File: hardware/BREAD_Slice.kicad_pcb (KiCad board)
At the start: 4 copper layers, 100 x 145 mm, 21 parts, among them J1 Conn_01x10_Socket, SW1 SW_DIP_x04, U1 AP63205

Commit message: did schematic
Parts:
- added J1: Screw_Terminal_01x02, TerminalBlock:TerminalBlock_MaiXu_MX126-5.0-02P_1x02_P5.00mm, F.Cu at (186.0, 121.2)
- added J3: PCIE-036-02-X-D-TH, KMLib_Connectors:SAMTEC_PCIE-036-02-X-D-TH, F.Cu at (144.0, 89.7)
- added J4: PCIE-036-02-X-D-TH, KMLib_Connectors:SAMTEC_PCIE-036-02-X-D-TH, F.Cu at (143.8, 67.7)
- added J5: PCIE-036-02-X-D-TH, KMLib_Connectors:SAMTEC_PCIE-036-02-X-D-TH, F.Cu at (143.8, 50.2)
- added J6: PCIE-036-02-X-D-TH, KMLib_Connectors:SAMTEC_PCIE-036-02-X-D-TH, F.Cu at (143.5, 33.2)
- added R1: 10k, Resistor_SMD:R_0603_1608Metric_Pad0.98x0.95mm_HandSolder, F.Cu at (145.8, 97.5)
- added R2: 10k, Resistor_SMD:R_0603_1608Metric_Pad0.98x0.95mm_HandSolder, F.Cu at (145.1, 75.2)
- added R3: 10k, Resistor_SMD:R_0603_1608Metric_Pad0.98x0.95mm_HandSolder, F.Cu at (144.8, 58.5)
- added R4: 10k, Resistor_SMD:R_0603_1608Metric_Pad0.98x0.95mm_HandSolder, F.Cu at (144.8, 40.5)
- added SW1: SW_SPDT, Button_Switch_THT:SW_Slide-03_Wuerth-WS-SLTV_10x2.5x6.4_P2.54mm, F.Cu at (177.2, 131.8)
- renumbered A2 to A1, J1 to J2, SW1 to SW2
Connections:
- net /slice_template/I2C0_CLK/GPIO21 renamed /DIR3
- net /slice_template/I2C0_SDA/GPIO20 renamed /STEP3
- A1 pad 10: /slice_template/GPIO7 -> /Stepper_card/SCL
- A1 pad 11: /slice_template/GPIO8 -> /STEP0
- A1 pad 12: /slice_template/GPIO9 -> /DIR0
- A1 pad 14: /slice_template/GPIO10 -> /CS0
- A1 pad 15: /slice_template/GPIO11 -> /STATUS0
- A1 pad 16: /slice_template/GPIO12 -> /STEP1
- A1 pad 17: /slice_template/GPIO13 -> /DIR1
- A1 pad 19: /slice_template/GPIO14 -> /CS1
- A1 pad 20: /slice_template/GPIO15 -> /STATUS1
- A1 pad 21: /slice_template/GPIO16 -> /STEP2
- A1 pad 22: /slice_template/GPIO17 -> /DIR2
- A1 pad 24: /slice_template/GPIO18 -> /CS2
- A1 pad 25: /slice_template/GPIO19 -> /STATUS2
- A1 pad 32: /slice_template/GPIO27_ADC1 -> /CS3
- A1 pad 34: /slice_template/GPIO28_ADC2 -> /STATUS3
- A1 pad 4: /slice_template/GPIO2 -> /SCLK
- A1 pad 5: /slice_template/GPIO3 -> /COPI
- A1 pad 6: /slice_template/GPIO4 -> /CIPO
- A1 pad 9: /slice_template/GPIO6 -> /Stepper_card/SDA

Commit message: more routing
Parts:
- removed SW1: SW_SPDT, Button_Switch_THT:SW_Slide-03_Wuerth-WS-SLTV_10x2.5x6.4_P2.54mm
- moved J4 10.3 mm to (151.0, 75.0)
- moved R2 9.68 mm to (151.5, 82.5), turned to -90 degrees
- moved J3 8.80 mm to (151.0, 95.0)
- moved J5 8.71 mm to (151.0, 55.0)
- moved R3 7.77 mm to (151.5, 62.5), turned to -90 degrees
- moved J6 7.72 mm to (151.0, 35.0)
- moved R1 7.62 mm to (151.5, 102.5), turned to -90 degrees
- moved R4 6.96 mm to (151.5, 42.5), turned to -90 degrees
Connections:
- J1 pad 1: Net-(J1-Pin_1) -> VM
- J3 pad A11: unconnected-(J3-PadA11) -> +3V3
- J3 pad A12: +3V3 -> VM
- J3 pad A3: /CIPO -> /SCLK
- J3 pad A5: /SCLK -> /CIPO
- J3 pad B11: unconnected-(J3-PadB11) -> +3V3
- J3 pad B12: +3V3 -> VM
- J3 pad B3: unconnected-(J3-PadB3) -> /SCLK
- J3 pad B4: unconnected-(J3-PadB4) -> /COPI
- J3 pad B5: unconnected-(J3-PadB5) -> /CIPO
- J3 pad B7: unconnected-(J3-PadB7) -> /Stepper_card/SDA
- J3 pad B8: unconnected-(J3-PadB8) -> /Stepper_card/SCL
- J4 pad A11: unconnected-(J4-PadA11) -> +3V3
- J4 pad A12: +3V3 -> VM
- J4 pad A3: /CIPO -> /SCLK
- J4 pad A5: /SCLK -> /CIPO
- J4 pad B11: unconnected-(J4-PadB11) -> +3V3
- J4 pad B12: +3V3 -> VM
- J4 pad B3: unconnected-(J4-PadB3) -> /SCLK
- J4 pad B4: unconnected-(J4-PadB4) -> /COPI
- J4 pad B5: unconnected-(J4-PadB5) -> /CIPO
- J4 pad B7: unconnected-(J4-PadB7) -> /Stepper_card/SDA
- J4 pad B8: unconnected-(J4-PadB8) -> /Stepper_card/SCL
- J5 pad A11: unconnected-(J5-PadA11) -> +3V3
- J5 pad A12: +3V3 -> VM
- J5 pad A3: /CIPO -> /SCLK
- J5 pad A5: /SCLK -> /CIPO
- J5 pad B11: unconnected-(J5-PadB11) -> +3V3
- J5 pad B12: +3V3 -> VM
- J5 pad B3: unconnected-(J5-PadB3) -> /SCLK
- J5 pad B4: unconnected-(J5-PadB4) -> /COPI
- J5 pad B5: unconnected-(J5-PadB5) -> /CIPO
- J5 pad B7: unconnected-(J5-PadB7) -> /Stepper_card/SDA
- J5 pad B8: unconnected-(J5-PadB8) -> /Stepper_card/SCL
- J6 pad A11: unconnected-(J6-PadA11) -> +3V3
- J6 pad A12: +3V3 -> VM
- J6 pad A3: /CIPO -> /SCLK
- J6 pad A5: /SCLK -> /CIPO
- J6 pad B11: unconnected-(J6-PadB11) -> +3V3
- J6 pad B12: +3V3 -> VM
- J6 pad B3: unconnected-(J6-PadB3) -> /SCLK
- J6 pad B4: unconnected-(J6-PadB4) -> /COPI
- J6 pad B5: unconnected-(J6-PadB5) -> /CIPO
- J6 pad B7: unconnected-(J6-PadB7) -> /Stepper_card/SDA
- J6 pad B8: unconnected-(J6-PadB8) -> /Stepper_card/SCL
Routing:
- net /SCLK: track 0.00 -> 126.7 mm
- net /COPI: track 0.00 -> 125.7 mm
- net VM: track 0.00 -> 121.4 mm
- net /CIPO: track 0.00 -> 120.8 mm
- net /Stepper_card/SDA: track 0.00 -> 112.3 mm
- net /Stepper_card/SCL: track 0.00 -> 111.4 mm
- net /STATUS2: track 0.00 -> 82.9 mm
- net /CS2: track 0.00 -> 82.5 mm
- net /DIR2: track 0.00 -> 79.1 mm
- net /STEP2: track 0.00 -> 77.6 mm
- net /STEP1: track 0.00 -> 63.3 mm
- net /DIR1: track 0.00 -> 58.6 mm
- net /CS1: track 0.00 -> 50.7 mm
- net /STEP0: track 0.00 -> 47.3 mm
- net /STATUS1: track 0.00 -> 46.4 mm
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
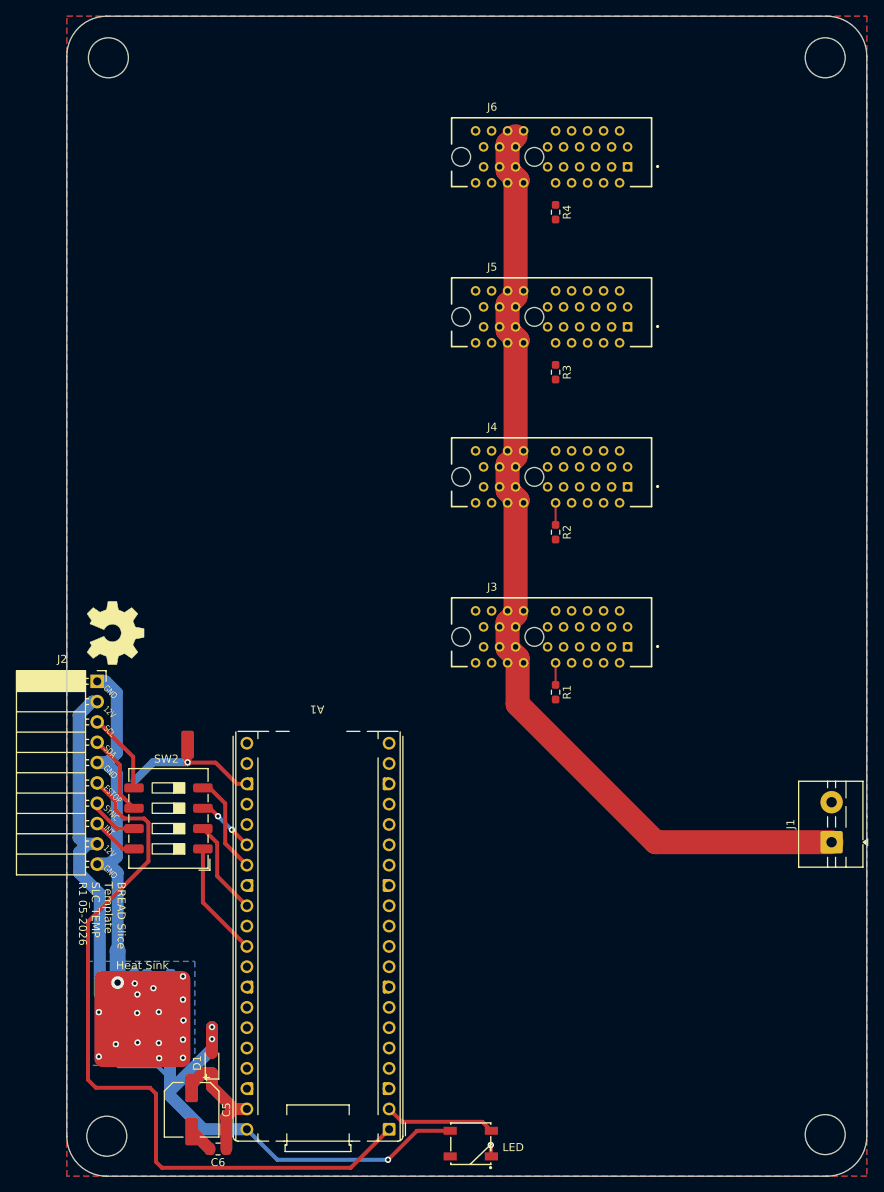
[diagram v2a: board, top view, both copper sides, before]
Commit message: finished initial routing
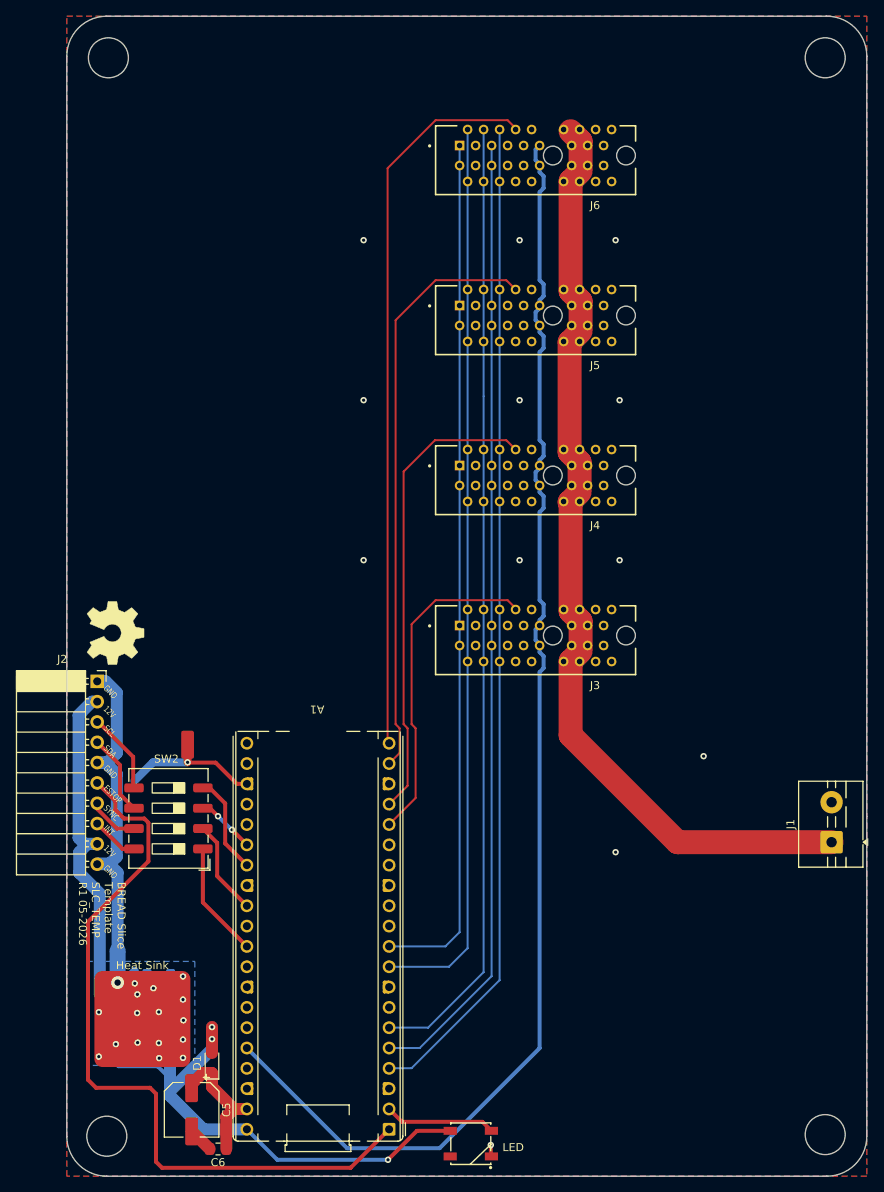
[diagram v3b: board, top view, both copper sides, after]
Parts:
- removed R1, R2, R3, R4: 10k, Resistor_SMD:R_0603_1608Metric_Pad0.98x0.95mm_HandSolder
- moved J3 2.24 mm to (149.0, 96.0), turned to 180 degrees
- moved J4 2.24 mm to (149.0, 76.0), turned to 180 degrees
- moved J5 2.24 mm to (149.0, 56.0), turned to 180 degrees
- moved J6 2.24 mm to (149.0, 36.0), turned to 180 degrees
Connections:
- A1 pad 11: /STEP0 -> /STEP3
- A1 pad 12: /DIR0 -> /STEP2
- A1 pad 14: /CS0 -> /STEP1
- A1 pad 15: /STATUS0 -> /STEP0
- A1 pad 16: /STEP1 -> /DIR0
- A1 pad 19: /CS1 -> /DIR2
- A1 pad 20: /STATUS1 -> /DIR3
- A1 pad 21: /STEP2 -> /CS3
- A1 pad 22: /DIR2 -> /CS2
- A1 pad 24: /CS2 -> /CS1
- A1 pad 25: /STATUS2 -> /CS0
- A1 pad 26: /STEP3 -> /slice_template/I2C0_SDA/GPIO20
- A1 pad 27: /DIR3 -> /slice_template/I2C0_CLK/GPIO21
- A1 pad 32: /CS3 -> /slice_template/GPIO27_ADC1
- A1 pad 34: /STATUS3 -> /slice_template/GPIO28_ADC2
- J3 pad A1: /STEP0 -> /Stepper_card/SCL
- J3 pad A10: /STATUS0 -> unconnected-(J3-PadA10)
- J3 pad A2: /DIR0 -> /Stepper_card/SDA
- J3 pad A3: /SCLK -> /CS0
- J3 pad A4: /COPI -> /CIPO
- J3 pad A5: /CIPO -> /COPI
- J3 pad A6: /CS0 -> /SCLK
- J3 pad A7: /Stepper_card/SDA -> /STEP0
- J3 pad A8: /Stepper_card/SCL -> /DIR0
- J3 pad A9: +3V3 -> unconnected-(J3-PadA9)
- J3 pad B1: /Stepper_card/nFAULT -> /Stepper_card/SCL
- J3 pad B2: unconnected-(J3-PadB2) -> /Stepper_card/SDA
- J3 pad B3: /SCLK -> unconnected-(J3-PadB3)
- J3 pad B4: /COPI -> /CIPO
- J3 pad B5: /CIPO -> /COPI
- J3 pad B6: unconnected-(J3-PadB6) -> /SCLK
- J3 pad B7: /Stepper_card/SDA -> unconnected-(J3-PadB7)
- J3 pad B8: /Stepper_card/SCL -> /Stepper_card/nFAULT
- J4 pad A1: /STEP1 -> /Stepper_card/SCL
- J4 pad A10: /STATUS1 -> unconnected-(J4-PadA10)
- J4 pad A2: /DIR1 -> /Stepper_card/SDA
- J4 pad A3: /SCLK -> /CS1
- J4 pad A4: /COPI -> /CIPO
- J4 pad A5: /CIPO -> /COPI
- J4 pad A6: /CS1 -> /SCLK
- J4 pad A7: /Stepper_card/SDA -> /STEP1
- J4 pad A8: /Stepper_card/SCL -> /DIR1
- J4 pad A9: +3V3 -> unconnected-(J4-PadA9)
- J4 pad B1: /Stepper_card1/nFAULT -> /Stepper_card/SCL
- J4 pad B2: unconnected-(J4-PadB2) -> /Stepper_card/SDA
- J4 pad B3: /SCLK -> unconnected-(J4-PadB3)
- J4 pad B4: /COPI -> /CIPO
- J4 pad B5: /CIPO -> /COPI
- J4 pad B6: unconnected-(J4-PadB6) -> /SCLK
- J4 pad B7: /Stepper_card/SDA -> unconnected-(J4-PadB7)
- J4 pad B8: /Stepper_card/SCL -> /Stepper_card1/nFAULT
- J5 pad A1: /STEP2 -> /Stepper_card/SCL
- J5 pad A10: /STATUS2 -> unconnected-(J5-PadA10)
- J5 pad A2: /DIR2 -> /Stepper_card/SDA
- J5 pad A3: /SCLK -> /CS2
- J5 pad A4: /COPI -> /CIPO
- J5 pad A5: /CIPO -> /COPI
- J5 pad A6: /CS2 -> /SCLK
- J5 pad A7: /Stepper_card/SDA -> /STEP2
- J5 pad A8: /Stepper_card/SCL -> /DIR2
- J5 pad A9: +3V3 -> unconnected-(J5-PadA9)
- J5 pad B1: /Stepper_card2/nFAULT -> /Stepper_card/SCL
- J5 pad B2: unconnected-(J5-PadB2) -> /Stepper_card/SDA
- J5 pad B3: /SCLK -> unconnected-(J5-PadB3)
- J5 pad B4: /COPI -> /CIPO
- J5 pad B5: /CIPO -> /COPI
- J5 pad B6: unconnected-(J5-PadB6) -> /SCLK
- J5 pad B7: /Stepper_card/SDA -> unconnected-(J5-PadB7)
- J5 pad B8: /Stepper_card/SCL -> /Stepper_card2/nFAULT
- J6 pad A1: /STEP3 -> /Stepper_card/SCL
- J6 pad A10: /STATUS3 -> unconnected-(J6-PadA10)
- J6 pad A2: /DIR3 -> /Stepper_card/SDA
- J6 pad A3: /SCLK -> /CS3
- J6 pad A4: /COPI -> /CIPO
- J6 pad A5: /CIPO -> /COPI
- J6 pad A6: /CS3 -> /SCLK
- J6 pad A7: /Stepper_card/SDA -> /STEP3
- J6 pad A8: /Stepper_card/SCL -> /DIR3
- J6 pad A9: +3V3 -> unconnected-(J6-PadA9)
- J6 pad B1: /Stepper_card3/nFAULT -> /Stepper_card/SCL
- J6 pad B2: unconnected-(J6-PadB2) -> /Stepper_card/SDA
- J6 pad B3: /SCLK -> unconnected-(J6-PadB3)
- J6 pad B4: /COPI -> /CIPO
- J6 pad B5: /CIPO -> /COPI
- J6 pad B6: unconnected-(J6-PadB6) -> /SCLK
- J6 pad B7: /Stepper_card/SDA -> unconnected-(J6-PadB7)
- J6 pad B8: /Stepper_card/SCL -> /Stepper_card3/nFAULT
- SW2 pad 3: /STEP3 -> /slice_template/I2C0_SDA/GPIO20
- SW2 pad 4: /DIR3 -> /slice_template/I2C0_CLK/GPIO21
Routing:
- net +3V3: track 0.00 -> 164.3 mm
- net /STEP3: track 7.41 -> 144.1 mm, vias 2 -> 0
- net /CS3: track 0.00 -> 98.1 mm
- net /STATUS2: track 82.9 -> 0.00 mm
- net /DIR3: track 12.5 -> 91.0 mm
- net /STATUS1: track 46.4 -> 0.00 mm
- net /STEP2: track 77.6 -> 121.7 mm
- net /STEP1: track 63.3 -> 98.6 mm
- net /STATUS0: track 34.5 -> 0.00 mm
- net /STEP0: track 47.3 -> 75.7 mm
- net /CS1: track 50.7 -> 65.7 mm
- net /CS0: track 35.6 -> 48.3 mm
- net /slice_template/I2C0_CLK/GPIO21: track 0.00 -> 12.5 mm
- net /slice_template/I2C0_SDA/GPIO20: track 0.00 -> 7.41 mm, vias 0 -> 2
- net VM: track 121.4 -> 115.9 mm
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
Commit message: added nFAULT line
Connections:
- A1 pad 32: /slice_template/GPIO27_ADC1 -> /nFAULT
- J3 pad B8: /Stepper_card/nFAULT -> /nFAULT
- J4 pad B8: /Stepper_card1/nFAULT -> /nFAULT
- J5 pad B8: /Stepper_card2/nFAULT -> /nFAULT
- J6 pad B8: /Stepper_card3/nFAULT -> /nFAULT
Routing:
- net /nFAULT: track 0.00 -> 137.8 mm
- net +3V3: track 164.3 -> 163.1 mm
- net GND: vias 30 -> 33
